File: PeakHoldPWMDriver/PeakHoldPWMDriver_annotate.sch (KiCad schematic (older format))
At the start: 77 parts, among them J1 Screw_Terminal_01x06, J2 Screw_Terminal_01x08, Q1 AO3400, Q10 AO3401A, Q11 AO3401A, Q12 BSP78, Q14 BSP78, Q17 AO3422, Q19 AO3422, Q2 AO3400, Q20 AO3401A, Q21 BSP78, Q22 AO3401A, Q23 BSP78, Q3 AO3400, Q4 AO3400, Q8 AO3422, Q9 AO3422, U10 74LS08, U11 74LS08, U2 LM78M05_TO220, U4 74LS32, U6 LM2901, U7 LTC6992, U8 74LS74, U9 74LS74

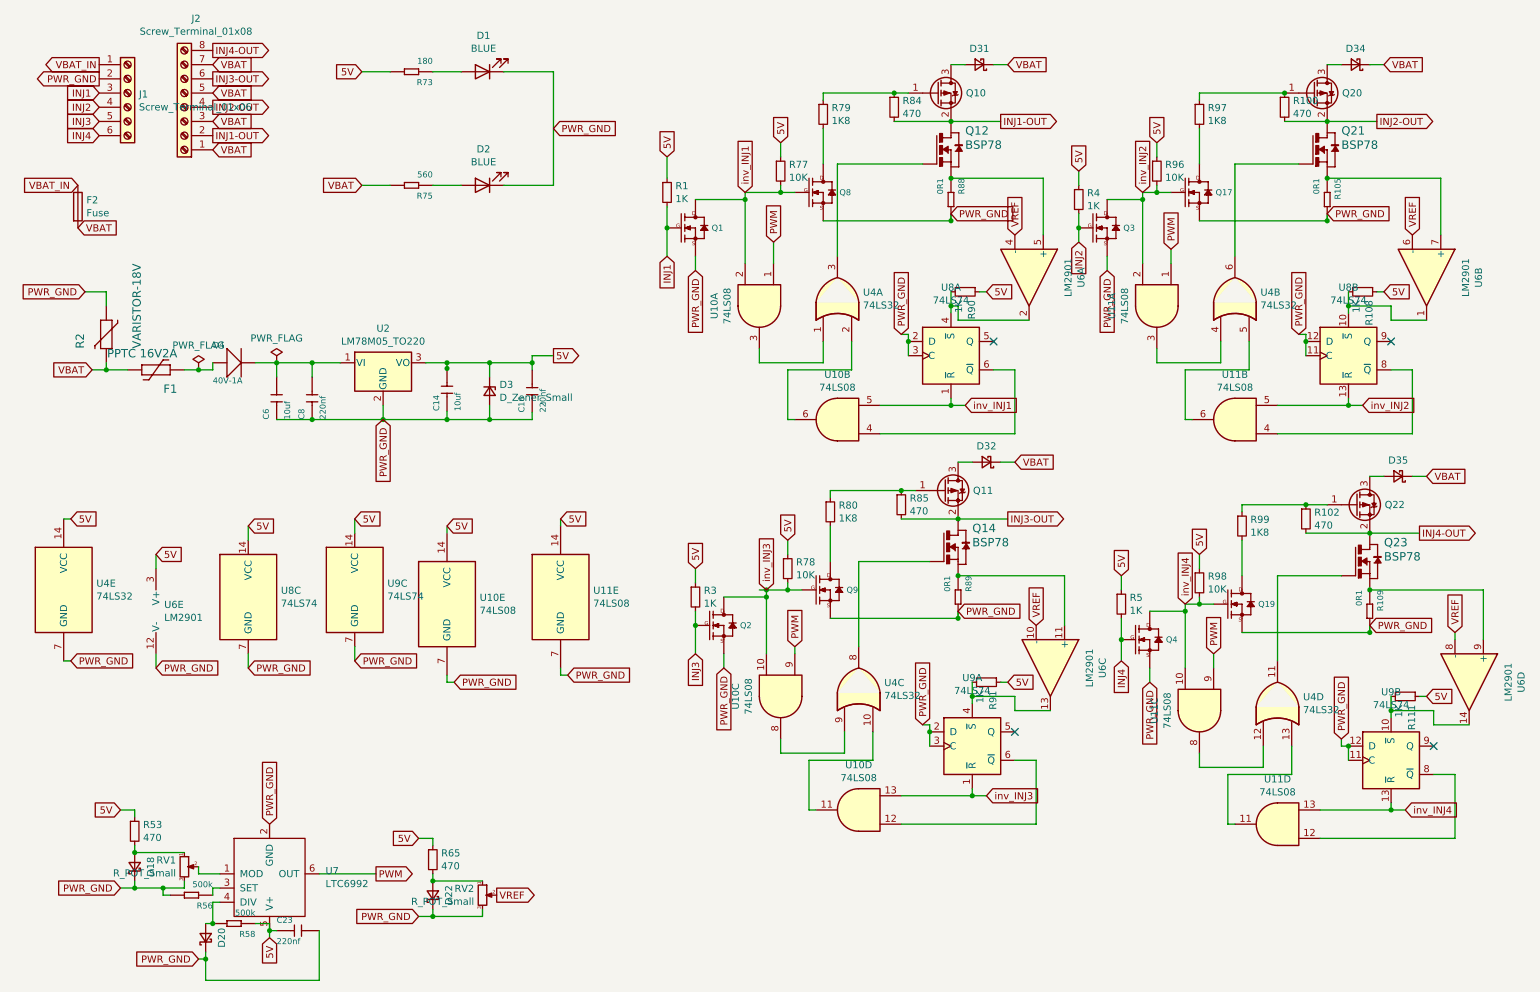
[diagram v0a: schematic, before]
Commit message: Cleaned and updated the SPECTRE V0.5 Created separate Peak and Hold board.
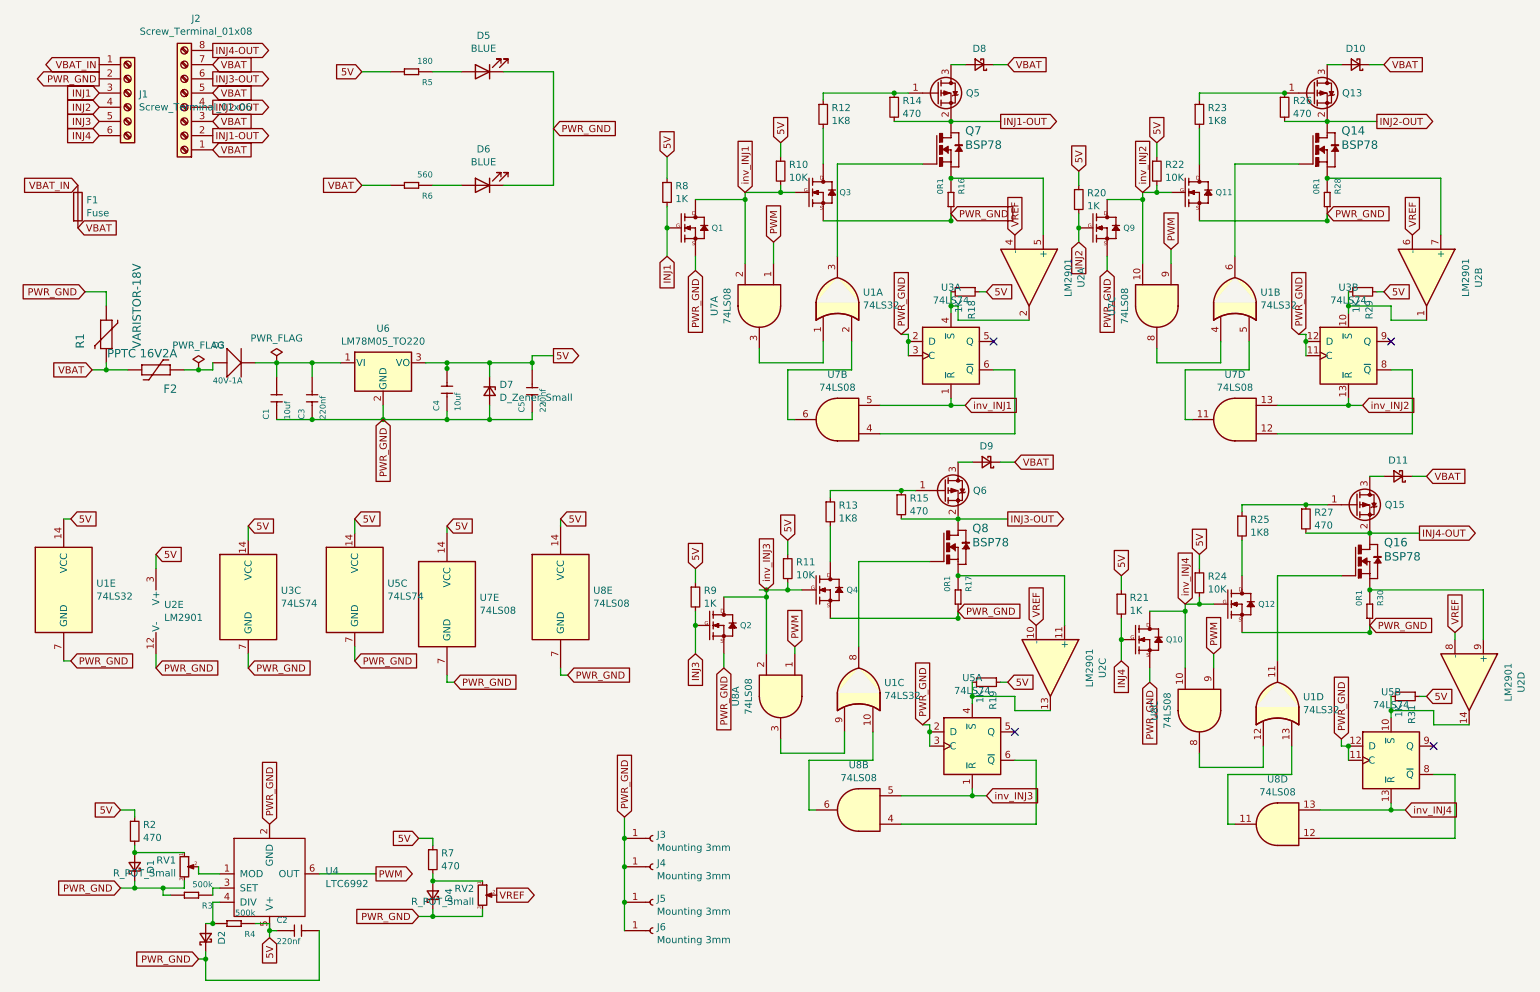
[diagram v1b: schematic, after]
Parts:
- added J3, J4, J5, J6: Mounting 3mm, MountingHole:MountingHole_3.2mm_M3_DIN965_Pad, symbol Connector:Conn_01x01_Female
- D10: renamed from D34; footprint Diode_SMD:D_SMA-SMB_Universal_Handsoldering -> Diode_SMD:D_SMA
- D11: renamed from D35; footprint Diode_SMD:D_SMA-SMB_Universal_Handsoldering -> Diode_SMD:D_SMA
- D3: renamed from D4; footprint Diode_SMD:D_SMA-SMB_Universal_Handsoldering -> Diode_SMD:D_SMA
- D8: renamed from D31; footprint Diode_SMD:D_SMA-SMB_Universal_Handsoldering -> Diode_SMD:D_SMA
- D9: renamed from D32; footprint Diode_SMD:D_SMA-SMB_Universal_Handsoldering -> Diode_SMD:D_SMA
- renumbered C6 to C1, C23 to C2, C8 to C3, C14 to C4, C16 to C5, D18 to D1, D20 to D2, D22 to D4, D1 to D5, D2 to D6, D3 to D7, F2 to F1, F1 to F2, Q4 to Q10, Q17 to Q11, Q19 to Q12, Q20 to Q13, Q21 to Q14, Q22 to Q15, Q23 to Q16, Q8 to Q3, Q9 to Q4, Q10 to Q5, Q11 to Q6, Q12 to Q7, Q14 to Q8, Q3 to Q9, R2 to R1, R77 to R10, R78 to R11, R79 to R12, R80 to R13, R84 to R14, R85 to R15, R88 to R16, R89 to R17, R90 to R18, R91 to R19, R53 to R2, R4 to R20, R5 to R21, R96 to R22, R97 to R23, R98 to R24, R99 to R25, R100 to R26, R102 to R27, R105 to R28, R108 to R29, R56 to R3, R109 to R30, R111 to R31, R58 to R4, R73 to R5, R75 to R6, R65 to R7, R1 to R8, R3 to R9, U4 to U1, U6 to U2, U8 to U3, U7 to U4, U9 to U5, U2 to U6, U10 to U7, U11 to U7, U10 to U8, U11 to U8
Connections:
- net PWM: now also U7.9, U8.1; no longer U7.1, U8.9
- net PWR_GND: now also J3.1 (Pin_1), J4.1 (Pin_1), J5.1 (Pin_1), J6.1 (Pin_1)
- net inv_INJ2: now also U7.10, U7.13; no longer U7.2, U7.5
- net inv_INJ3: now also U8.2, U8.5; no longer U8.10, U8.13
- net at U5.6 (~Q): now also U8.4; no longer U8.12
- net at U1.9: now also U8.3; no longer U8.8
- net at U1.10: now also U8.6; no longer U8.11
- net at U3.8 (~Q): now also U7.12; no longer U7.4
- net at U1.4: now also U7.8; no longer U7.3
- net at U1.5: now also U7.11; no longer U7.6
